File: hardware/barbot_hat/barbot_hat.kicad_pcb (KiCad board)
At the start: 2 copper layers, 65 x 56 mm, 10 parts, among them J1 GPIO, J2 Conn_01x02, J3 Conn_01x02, J4 Conn_01x02, J5 Conn_01x02

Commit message: Work on layout
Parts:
- added A2: Pololu_Breakout_A4988, Module:Pololu_Breakout-16_15.2x20.3mm, F.Cu at (114.7, 59.8)
- added C2: C_Polarized, Capacitor_THT:CP_Radial_D10.0mm_P5.00mm, F.Cu at (122.0, 82.5)
- added C3: C, Capacitor_SMD:C_0805_2012Metric_Pad1.18x1.45mm_HandSolder, B.Cu at (128.0, 55.5)
- added D1: WS2812B, LED_SMD:LED_WS2812B_PLCC4_5.0x5.0mm_P3.2mm, F.Cu at (125.0, 54.0)
- added D2: WS2812B, LED_SMD:LED_WS2812B_PLCC4_5.0x5.0mm_P3.2mm, F.Cu at (117.0, 54.0)
- added D3: D, Diode_THT:D_DO-27_P5.08mm_Vertical_AnodeUp, F.Cu at (139.0, 54.0)
- added G***: LOGO, LOGO, F.Cu at (135.7, 70.9)
- added J6: Conn_01x02, Connector_PinHeader_2.54mm:PinHeader_1x02_P2.54mm_Horizontal, F.Cu at (115.0, 89.3)
- added J7: Conn_01x03, Connector_PinHeader_2.54mm:PinHeader_1x03_P2.54mm_Horizontal, F.Cu at (110.4, 58.5)
- added J8: Conn_01x04, Connector_PinHeader_2.54mm:PinHeader_1x04_P2.54mm_Horizontal, F.Cu at (110.4, 72.5)
- added J9: Screw_Terminal_01x02, TerminalBlock:TerminalBlock_bornier-2_P5.08mm, F.Cu at (104.0, 78.5)
- added U3: MCP1416, Package_TO_SOT_SMD:SOT-23-5, B.Cu at (130.0, 86.0)
- added U4: MCP1416, Package_TO_SOT_SMD:SOT-23-5, B.Cu at (137.9, 85.9)
- added U5: MCP1416, Package_TO_SOT_SMD:SOT-23-5, B.Cu at (145.9, 86.0)
- added U6: MCP1416, Package_TO_SOT_SMD:SOT-23-5, B.Cu at (153.9, 86.0)
- added U7: MCP1416, Package_TO_SOT_SMD:SOT-23-5, B.Cu at (113.7, 86.0)
- added U8: SN74LV1T34DBV, Package_TO_SOT_SMD:SOT-23-5, B.Cu at (124.0, 54.5)
- added U9: AMS1117CD-5.0, Package_TO_SOT_SMD:TO-252-3_TabPin2, F.Cu at (6.42, 3.67)
- moved J2 24.5 mm to (131.2, 89.5)
- moved J5 21.0 mm to (155.2, 89.5)
- moved J3 9.33 mm to (139.2, 89.5)
- moved J4 5.85 mm to (147.2, 89.5)
- moved U2 4.30 mm to (153.0, 65.1)
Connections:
- J1 pad 15: /GPIO22 -> /GPIO22 / NEOPIXEL_IN
- J2 pad 1: unconnected-(J2-Pin_1-Pad1) -> GND
- J2 pad 2: unconnected-(J2-Pin_2-Pad2) -> Net-(J2-Pin_2)
- J3 pad 1: unconnected-(J3-Pin_1-Pad1) -> GND
- J3 pad 2: unconnected-(J3-Pin_2-Pad2) -> Net-(J3-Pin_2)
- J4 pad 1: unconnected-(J4-Pin_1-Pad1) -> GND
- J4 pad 2: unconnected-(J4-Pin_2-Pad2) -> Net-(J4-Pin_2)
- J5 pad 1: unconnected-(J5-Pin_1-Pad1) -> GND
- J5 pad 2: unconnected-(J5-Pin_2-Pad2) -> Net-(J5-Pin_2)
- U2 pad 13: unconnected-(U2-GND-Pad13) -> GND
- U2 pad 14: unconnected-(U2-5V-Pad14) -> Net-(D3-K)
- U2 pad 2: unconnected-(U2-GPIO3-Pad2) -> /PUMP_CTRL3
- U2 pad 20: unconnected-(U2-GND-Pad20) -> GND
- U2 pad 3: unconnected-(U2-GPIO4-Pad3) -> /PUMP_CTRL2
- U2 pad 4: unconnected-(U2-GPIO5-Pad4) -> /PUMP_CTRL1
- U2 pad 5: unconnected-(U2-GPIO6-Pad5) -> /PUMP_CTRL0
- U2 pad 6: unconnected-(U2-GPIO7-Pad6) -> /MOTOR_Z
- U2 pad 7: unconnected-(U2-GPIO21-Pad7) -> /MOTOR_X_DIR
- U2 pad 8: unconnected-(U2-GPIO20-Pad8) -> /MOTOR_X_STEP
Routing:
- net +5V: track 0.00 -> 90.2 mm, vias 0 -> 2
- net +12V: track 0.00 -> 68.8 mm, vias 0 -> 5
- net +3V3: track 0.00 -> 60.4 mm
- net /MOTOR_Z: track 0.00 -> 59.2 mm, vias 0 -> 1
- net Net-(D3-K): track 0.00 -> 46.3 mm
- net /PUMP_CTRL0: track 0.00 -> 45.8 mm, vias 0 -> 1
- net /PUMP_CTRL1: track 0.00 -> 41.0 mm, vias 0 -> 1
- net /PUMP_CTRL2: track 0.00 -> 36.3 mm, vias 0 -> 1
- net /PUMP_CTRL3: track 0.00 -> 33.8 mm, vias 0 -> 1
- net /MOTOR_X_STEP: track 0.00 -> 28.3 mm
- net /MOTOR_X_DIR: track 0.00 -> 20.0 mm
- net GND: track 0.00 -> 12.3 mm
- net /GPIO22 / NEOPIXEL_IN: track 0.00 -> 7.45 mm
- net Net-(D1-DOUT): track 0.00 -> 5.64 mm
- net /NEOPIXEL_OUT: track 0.00 -> 4.31 mm
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- added copper zone on B.Cu, net GND
- added copper zone on F.Cu, net GND
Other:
- board text added: "GND 12V"
- board text added: "M0"
- board text added: "M1"
- board text added: "M2"
- board text added: "M3"
- board text added: "MOTORS BARBOT 12V | GND ${CURRENT_DATE}"
- board text added: "Z"
- board text removed: "PoE"

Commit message: Add stepper ref image to schematic
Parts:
- removed U9: AMS1117CD-5.0, Package_TO_SOT_SMD:TO-252-3_TabPin2
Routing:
- net +12V: track 68.8 -> 66.7 mm
- net +5V: track 90.2 -> 89.7 mm

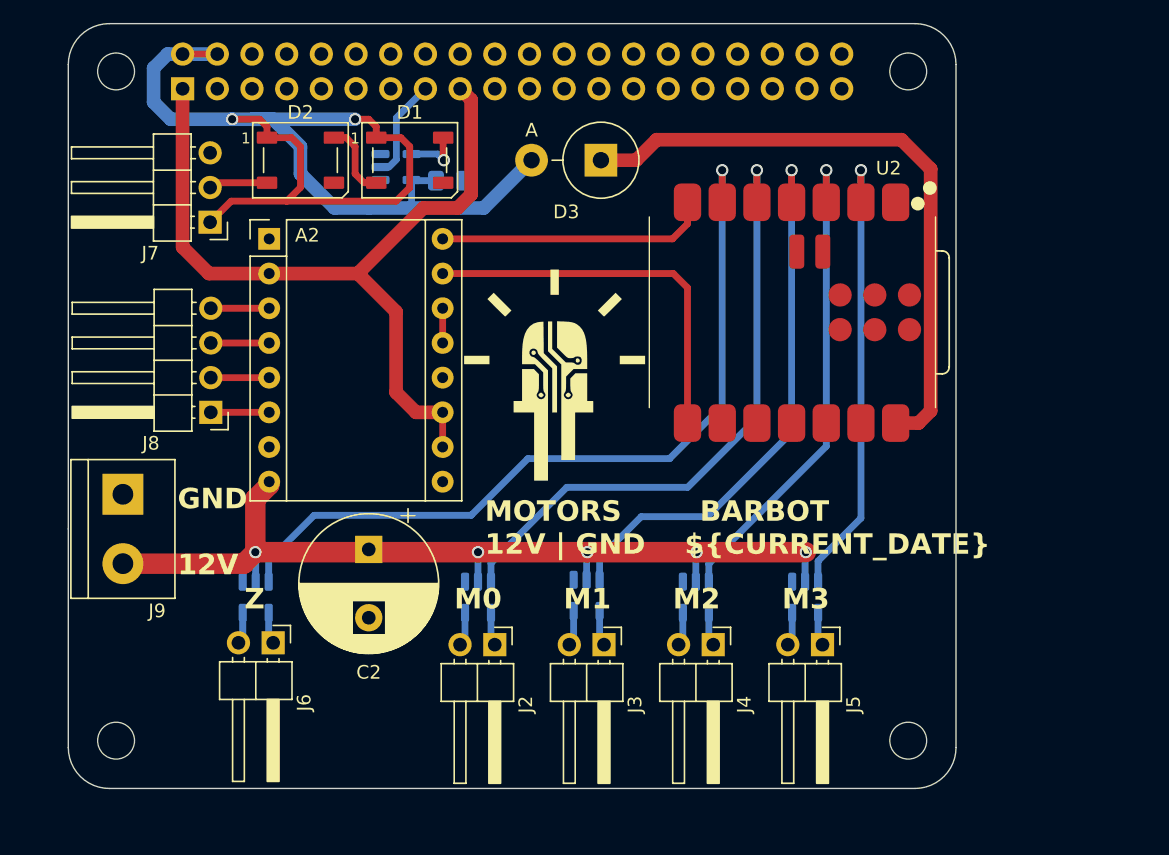
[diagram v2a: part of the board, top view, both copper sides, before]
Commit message: Change power delivery, update logo
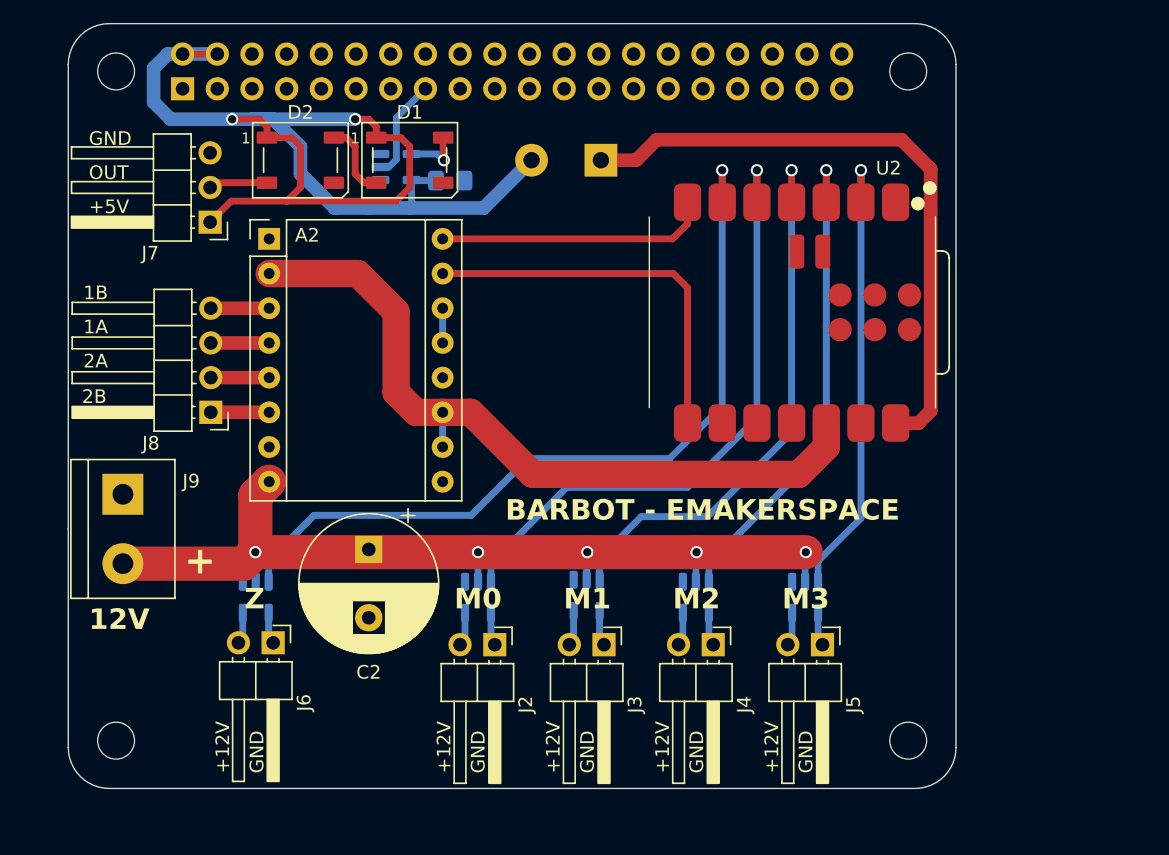
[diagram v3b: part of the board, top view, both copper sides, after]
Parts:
- D3: moved to B.Cu
- moved G*** 0.94 mm to (136.0, 70.0)
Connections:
- net Net-(A2-1A) renamed /1A
- net Net-(A2-1B) renamed /1B
- net Net-(A2-2A) renamed /2A
- net Net-(A2-2B) renamed /2B
- J1 pad 1: +3V3 -> unconnected-(J1-Pin_1-Pad1)
- J1 pad 17: +3V3 -> unconnected-(J1-Pin_17-Pad17)
- U2 pad 12: unconnected-(U2-3V3-Pad12) -> +3V3
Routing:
- net +3V3: track 60.4 -> 55.5 mm
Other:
- board text added: "${CURRENT_DATE}"
- board text added: "+"
- board text added: "+12V"
- board text added: "+5V"
- board text added: "12V"
- board text added: "1A"
- board text added: "1B"
- board text added: "2A"
- board text added: "2B"
- board text added: "BARBOT"
- board text added: "BARBOT - EMAKERSPACE"
- board text added: "BATCH"
- board text added: "CONTROLLER BOARD"
- board text added: "DATE"
- board text added: "GND"
- board text added: "OUT"
- board text added: "REVISION 1.0"
- board text added: "e734c4f"
- board text removed: "GND 12V"
- board text removed: "MOTORS BARBOT 12V | GND ${CURRENT_DATE}"

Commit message: Update front silk
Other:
- board text added: "BARBOT.EMAKERSPACE.CH"
- board text removed: "BARBOT - EMAKERSPACE"
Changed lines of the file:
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@@
 		)
 	)
-	(gr_text "BARBOT - EMAKERSPACE"
+	(gr_text "BARBOT.EMAKERSPACE.CH"
 		(at 132 80.5 0)
 		(layer "F.SilkS" knockout)

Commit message: Update images and readme
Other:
- board text removed: "e734c4f"
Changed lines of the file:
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@@
 	)
 	(gr_rect
-		(start 144.253673 72.514122)
-		(end 135.642678 74.645063)
+		(start 135.642678 72.514122)
+		(end 144.253673 74.645063)
 		(stroke
 			(width 0)
@@
 	)
 	(gr_rect
-		(start 159.948176 65.395063)
-		(end 134.948176 80.145063)
+		(start 134.948176 65.395063)
+		(end 159.948176 80.145063)
 		(stroke
 			(width 0.3)
@@
 	)
 	(gr_rect
-		(start 151.753673 77.514122)
-		(end 135.642678 79.645063)
+		(start 135.642678 77.514122)
+		(end 151.753673 79.645063)
 		(stroke
 			(width 0)
@@
 		(layer "B.SilkS")
 		(effects
-			(font
-				(size 1.5 1.5)
-				(thickness 0.3)
-				(bold yes)
-			)
-			(justify left bottom mirror)
-		)
-	)
-	(gr_text "e734c4f"
-		(at 132.5 80.5 270)
-		(layer "B.SilkS")
-		(effects
